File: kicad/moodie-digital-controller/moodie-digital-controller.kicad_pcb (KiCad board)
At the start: 2 copper layers, 60 x 26 mm, 8 parts, among them J1 Barrel_Jack, J2 Conn_01x03_Female, U1 WEMOS_D1_MINI

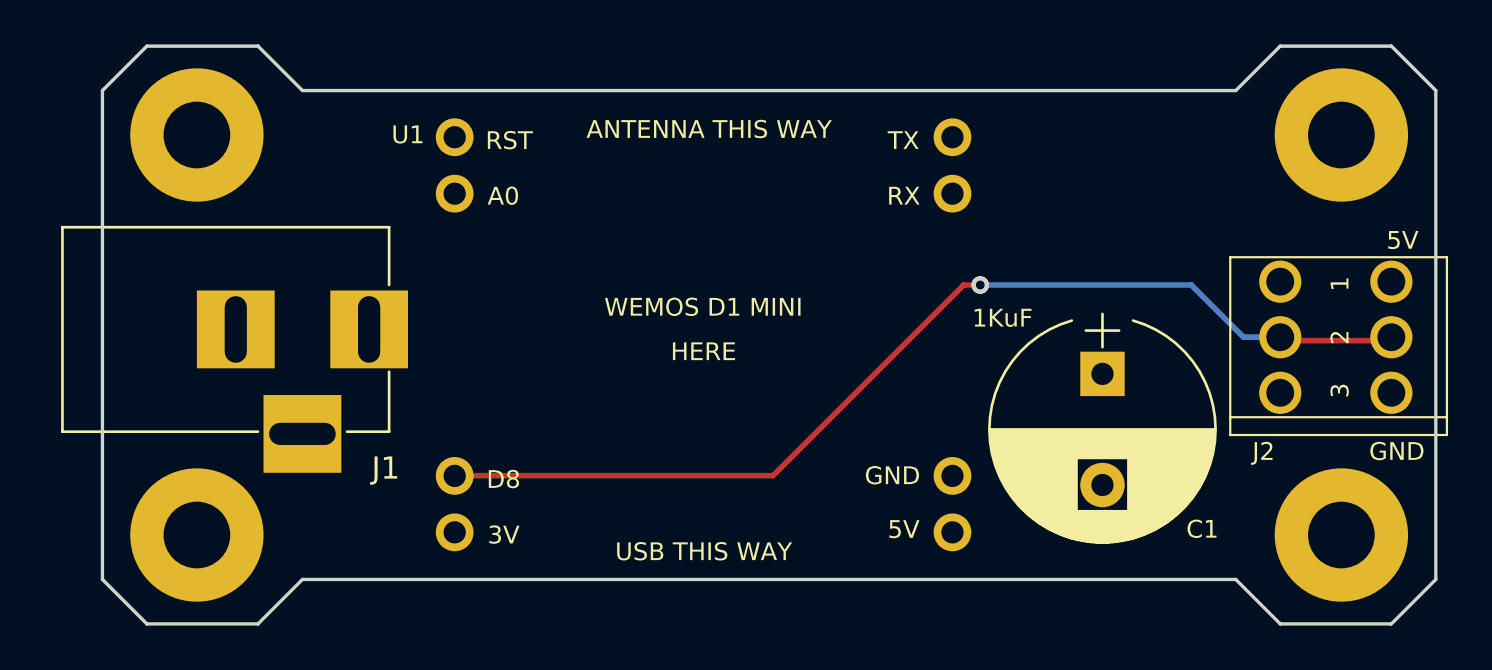
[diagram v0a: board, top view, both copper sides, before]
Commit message: Tidyup (#1)
* Added initial fuse (it's too big)

* Fix link, remove DS_Store
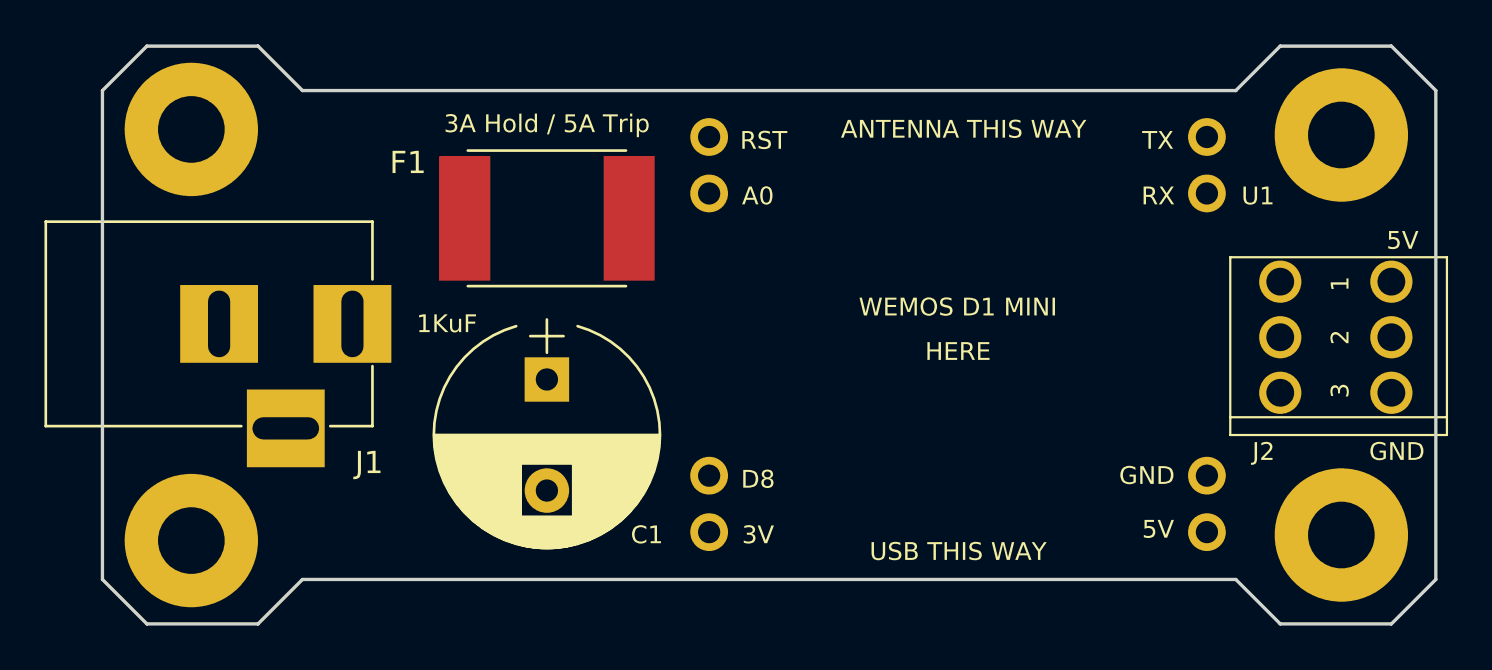
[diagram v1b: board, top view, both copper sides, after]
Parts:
- added F1: 3A Hold / 5A Trip, Fuse_Holders_and_Fuses:Fuse_SMD2920, F.Cu at (67.0, 91.8)
- moved C1 25.0 mm to (67.0, 99.0)
- moved U1 11.5 mm to (85.5, 96.8)
- moved J1 0.79 mm to (58.2, 96.5)
- moved REF** 0.35 mm to (51.0, 106.2)
- moved REF** 0.35 mm to (51.0, 87.8)
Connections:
- J1 pad 1: +5V -> Net-(F1-Pad2)
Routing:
- net /D8: track 46.9 -> 0.15 mm, vias 1 -> 0
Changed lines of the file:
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@@
     (thickness 1.6)
     (drawings 21)
-    (tracks 9)
+    (tracks 1)
     (zones 0)
-    (modules 8)
-    (nets 9)
+    (modules 9)
+    (nets 10)
   )
   (page A4)
@@
     (35 F.Paste user)
     (36 B.SilkS user)
-    (37 F.SilkS user hide)
+    (37 F.SilkS user)
     (38 B.Mask user)
     (39 F.Mask user)
@@
   (setup
     (last_trace_width 0.25)
+    (user_trace_width 0.5)
     (trace_clearance 0.2)
     (zone_clearance 0.508)
@@
   (net 7 "Net-(U1-Pad2)")
   (net 8 "Net-(U1-Pad8)")
+  (net 9 "Net-(F1-Pad2)")
   (net_class Default "This is the default net class."
     (clearance 0.2)
@@
     (add_net /D8)
     (add_net GND)
+    (add_net "Net-(F1-Pad2)")
     (add_net "Net-(U1-Pad1)")
     (add_net "Net-(U1-Pad10)")
@@
   )
   (module Mounting_Holes:MountingHole_3mm_Pad (layer F.Cu)
-    (at 51.25 106)
+    (at 51 106.25)
     (descr "Mounting Hole 3mm")
     (tags "mounting hole 3mm")
@@
   )
   (module Mounting_Holes:MountingHole_3mm_Pad locked (layer F.Cu)
-    (at 51.25 88)
+    (at 51 87.75)
     (descr "Mounting Hole 3mm")
     (tags "mounting hole 3mm")
@@
   )
   (module Capacitors_THT:CP_Radial_D10.0mm_P5.00mm (layer F.Cu)
-    (at 92 98.75 270)
+    (at 67 99 270)
     (descr "CP, Radial series, Radial, pin pitch=5.00mm, , diameter=10mm, Electrolytic Capacitor")
     (tags "CP Radial series Radial pin pitch 5.00mm  diameter 10mm Electrolytic Capacitor")
@@
   )
   (module Custom_Parts:WeMos_D1_Mini_Minimal_Connector (layer F.Cu)
-    (at 74.05 96.76)
-    (fp_text reference U1 (at -13.3 -8.76) (layer F.SilkS)
+    (at 85.5 96.75)
+    (fp_text reference U1 (at 13.5 -6) (layer F.SilkS)
       (effects (font (size 0.8 0.8) (thickness 0.1)))
     )
@@
   )
   (module Connectors:BARREL_JACK (layer F.Cu)
-    (at 59 96.75)
+    (at 58.25 96.5)
     (descr "DC Barrel Jack")
     (tags "Power Jack")
@@
       (net 1 GND))
     (pad 1 thru_hole rect (at 0 0) (size 3.5 3.5) (drill oval 1 3) (layers *.Cu *.Mask)
+      (net 9 "Net-(F1-Pad2)"))
+  )
+  (module Fuse_Holders_and_Fuses:Fuse_SMD2920 (layer F.Cu)
+    (at 67 91.75 180)
+    (descr "Fuse, 2920 chip size")
+    (tags "Fuse SMD2920")
+    (attr smd)
+    (fp_text reference F1 (at 6.25 2.5 180) (layer F.SilkS)
+      (effects (font (size 1 1) (thickness 0.15)))
+    )
+    (fp_text value "3A Hold / 5A Trip" (at 0 4.25 180) (layer F.SilkS)
+      (effects (font (size 0.8 0.8) (thickness 0.1)))
+    )
+    (fp_line (start -3.56 3.05) (end 3.56 3.05) (layer F.SilkS) (width 0.12))
+    (fp_line (start -3.56 -3.05) (end 3.56 -3.05) (layer F.SilkS) (width 0.12))
+    (fp_line (start -5.1 -3.3) (end 5.1 -3.3) (layer F.CrtYd) (width 0.05))
+    (fp_line (start -5.1 3.3) (end 5.1 3.3) (layer F.CrtYd) (width 0.05))
+    (fp_line (start -5.1 -3.3) (end -5.1 3.3) (layer F.CrtYd) (width 0.05))
+    (fp_line (start 5.1 -3.3) (end 5.1 3.3) (layer F.CrtYd) (width 0.05))
+    (fp_line (start -3.7 2.55) (end -3.7 -2.55) (layer F.Fab) (width 0.1))
+    (fp_line (start 3.7 2.55) (end -3.7 2.55) (layer F.Fab) (width 0.1))
+    (fp_line (start 3.7 -2.55) (end 3.7 2.55) (layer F.Fab) (width 0.1))
+    (fp_line (start -3.7 -2.55) (end 3.7 -2.55) (layer F.Fab) (width 0.1))
+    (pad 2 smd rect (at 3.7 0 270) (size 5.6 2.3) (layers F.Cu F.Paste F.Mask)
+      (net 9 "Net-(F1-Pad2)"))
+    (pad 1 smd rect (at -3.7 0 270) (size 5.6 2.3) (layers F.Cu F.Paste F.Mask)
       (net 2 +5V))
   )
@@
   (gr_line (start 49 84) (end 54 84) (layer Edge.Cuts) (width 0.15))
   (gr_line (start 47 86) (end 47 108) (layer Edge.Cuts) (width 0.15))
-  (segment (start 77.17 103.33) (end 62.8 103.33) (width 0.25) (layer F.Cu) (net 3))
-  (segment (start 105 97.25) (end 100 97.25) (width 0.25) (layer F.Cu) (net 3))
   (segment (start 100 97.75) (end 100 97.9) (width 0.25) (layer B.Cu) (net 3))
-  (segment (start 98.35 97.1) (end 100 97.1) (width 0.25) (layer B.Cu) (net 3))
-  (segment (start 96 94.75) (end 98.35 97.1) (width 0.25) (layer B.Cu) (net 3))
-  (via (at 86.5 94.75) (size 0.8) (drill 0.4) (layers F.Cu B.Cu) (net 3))
-  (segment (start 96 94.75) (end 86.5 94.75) (width 0.25) (layer B.Cu) (net 3))
-  (segment (start 86.5 94.75) (end 85.75 94.75) (width 0.25) (layer F.Cu) (net 3))
-  (segment (start 85.75 94.75) (end 77.17 103.33) (width 0.25) (layer F.Cu) (net 3))
   (zone (net 2) (net_name +5V) (layer F.Cu) (hatch edge 0.508)
     (connect_pads (clearance 0.508))
